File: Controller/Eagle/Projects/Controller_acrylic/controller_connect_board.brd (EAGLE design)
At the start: 185 x 33 mm, 13 parts, among them J1 GIMBAL_3PIN_MATCH_TDOCU, J2 GIMBAL_3PIN_MATCH_TDOCU, J3 GIMBAL_3PIN_MATCH_TDOCU, J4 GIMBAL_3PIN_MATCH_TDOCU, J5 GIMBAL_3PIN_MATCH_TDOCU

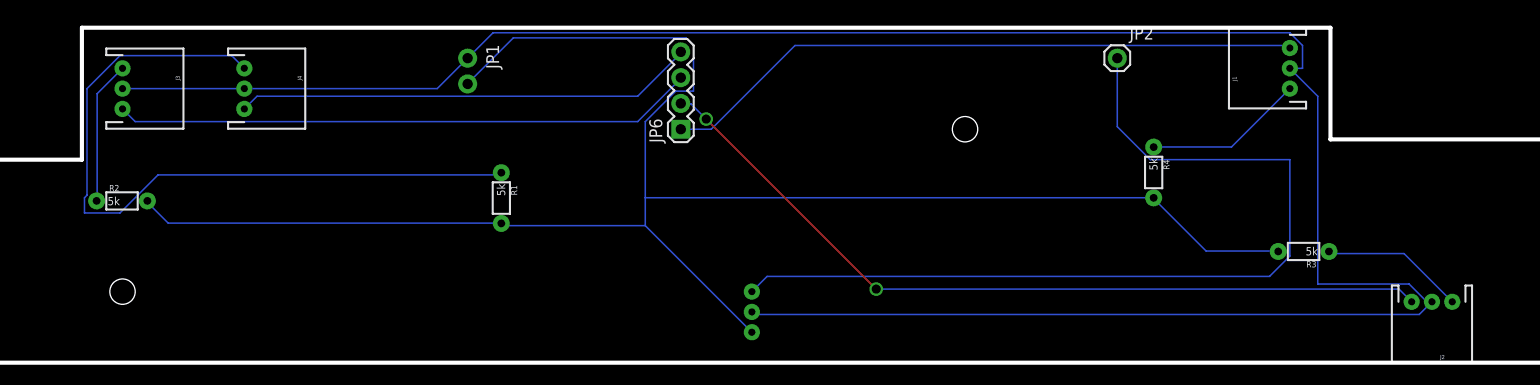
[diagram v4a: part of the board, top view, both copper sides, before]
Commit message: First test of connector board Ground and VDD were reversed on gimbal pins Made holes bigger
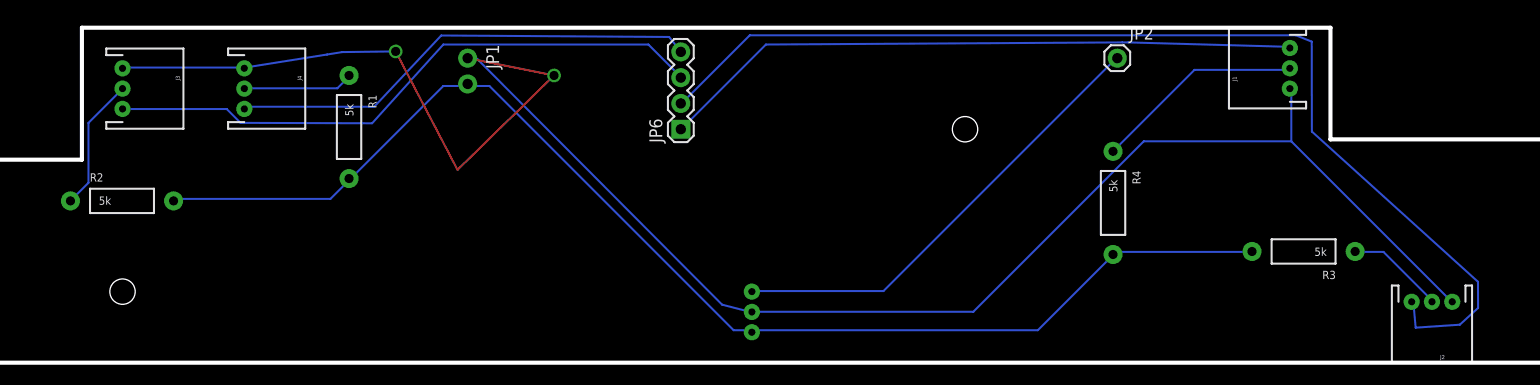
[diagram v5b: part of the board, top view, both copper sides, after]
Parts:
- J1, J2, J3, J4: value GIMBAL_3PIN_MATCH_TDOCU -> JST_3PIN_GND_VDD_SIG; device Controller:JST-3-PTH -> Controller:JST-3-PTH-REVERSE
- R1, R2, R3, R4: device SparkFun-Resistors:1/6W-RES -> SparkFun-Resistors:AXIAL-0.4
- moved R1 16.6 mm to (93.3, 45.2)
- moved R4 5.00 mm to (168.6, 37.7)
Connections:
- net N$5 renamed PITCH
- net N$6 renamed ROLL
- net N$7 renamed THROTTLE
- net N$8 renamed YAW
- net 3.3V: now also R1.P$2, R2.P$2, R3.P$2, R4.P$2; no longer R1.2, R2.2, R3.2, R4.2
- net GND: now also J1.1, J2.1, J3.1, J4.1; no longer J1.2, J2.2, J3.2, J4.2
- net N$1: now also J4.2, R1.P$1; no longer J4.1, R1.1
- net N$2: now also J3.2, R2.P$1; no longer J3.1, R2.1
- net N$3: now also J2.2, R3.P$1; no longer J2.1, R3.1
- net N$4: now also J1.2, R4.P$1; no longer J1.1, R4.1
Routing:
- net N$1: track 72.5 -> 10.9 mm
- net 3.3V: track 174.7 -> 124.8 mm
- net N$9: track 89.0 -> 45.5 mm
- net GND: track 224.4 -> 188.1 mm, vias 0 -> 2
- net ROLL: track 80.1 -> 108.0 mm, vias 2 -> 0
- net N$4: track 15.8 -> 20.8 mm
- net N$3: track 14.2 -> 9.69 mm
- net THROTTLE: track 57.4 -> 60.4 mm
- net YAW: track 45.4 -> 46.9 mm
- net N$2: track 14.1 -> 13.2 mm

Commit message: FORGOT THE BUTTON WOW WOW I...WOW
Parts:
- added BUTTON: (no value), SparkFun-Connectors:1X01
- added R5: ~10k, SparkFun-Resistors:AXIAL-0.4
- added U$2: BUTTON-TACTILE-SQUARE, Controller:BUTTON-TACTILE-SQUARE-ADAFRUIT1010
- R1, R2, R3, R4: value 5k -> 5k-8.2k
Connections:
- new net N$6: BUTTON.1, R5.P$2, U$2.S, U$2.S2
- net 3.3V: now also U$2.P, U$2.P2
- net GND: now also R5.P$1
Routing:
- net N$6: track 0.00 -> 36.9 mm
- net GND: track 188.1 -> 209.4 mm
- net N$9: track 45.5 -> 56.9 mm
- net 3.3V: track 124.8 -> 132.6 mm
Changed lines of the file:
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@@
 <element name="J3" library="Controller" package="JST-3-PTH-REVERSE" value="JST_3PIN_GND_VDD_SIG" x="71" y="49" rot="R270"/>
 <element name="J4" library="Controller" package="JST-3-PTH-REVERSE" value="JST_3PIN_GND_VDD_SIG" x="83" y="49" rot="R270"/>
-<element name="R1" library="SparkFun-Resistors" package="AXIAL-0.4" value="5k" x="93.318003125" y="45.219046875" rot="R270"/>
-<element name="R2" library="SparkFun-Resistors" package="AXIAL-0.4" value="5k" x="70.949403125" y="37.939940625"/>
-<element name="R3" library="SparkFun-Resistors" package="AXIAL-0.4" value="5k" x="187.352325" y="32.957490625" rot="R180"/>
-<element name="R4" library="SparkFun-Resistors" package="AXIAL-0.4" value="5k" x="168.58266875" y="37.739028125" rot="R270"/>
+<element name="R1" library="SparkFun-Resistors" package="AXIAL-0.4" value="5k-8.2k" x="93.318003125" y="45.219046875" rot="R270"/>
+<element name="R2" library="SparkFun-Resistors" package="AXIAL-0.4" value="5k-8.2k" x="70.949403125" y="37.939940625"/>
+<element name="R3" library="SparkFun-Resistors" package="AXIAL-0.4" value="5k-8.2k" x="187.352325" y="32.957490625" rot="R180"/>
+<element name="R4" library="SparkFun-Resistors" package="AXIAL-0.4" value="5k-8.2k" x="168.58266875" y="37.739028125" rot="R270"/>
 <element name="JP6" library="SparkFun-Connectors" package="1X04" value="" x="126" y="45" rot="R90"/>
 <element name="JP1" library="SparkFun-Connectors" package="1X02_NO_SILK" value="" x="105" y="52" rot="R270"/>
@@
 <element name="JP2" library="SparkFun-Connectors" package="1X01" value="" x="169" y="52"/>
 <element name="U$1" library="Controller" package="CONNECTOR_BOARD_OUTLINE" value="" x="0" y="0"/>
+<element name="U$2" library="Controller" package="BUTTON-TACTILE-SQUARE-ADAFRUIT1010" value="BUTTON-TACTILE-SQUARE" x="152.719" y="31.166" rot="R180"/>
+<element name="BUTTON" library="SparkFun-Connectors" package="1X01" value="" x="156.66" y="49.897"/>
+<element name="R5" library="SparkFun-Resistors" package="AXIAL-0.4" value="~10k" x="143.013" y="49.942"/>
 </elements>
 <signals>
@@
 <wire x1="82.855" y1="51.075" x2="83" y2="51" width="0.2" layer="16"/>
 <wire x1="130.071" y1="27.715" x2="132.795" y2="27.013" width="0.2" layer="16"/>
-<wire x1="105.968" y1="51.9" x2="130.071" y2="27.715" width="0.2" layer="16"/>
+<wire x1="105.968" y1="51.9" x2="122.40503125" y2="35.40705" width="0.2" layer="16"/>
+<wire x1="122.40503125" y1="35.40705" x2="130.071" y2="27.715" width="0.2" layer="16"/>
 <wire x1="132.795" y1="27.013" x2="133" y2="27" width="0.2" layer="16"/>
 <wire x1="105.968" y1="51.9" x2="105" y2="52" width="0.2" layer="16"/>
@@
 <wire x1="83.082" y1="51.075" x2="83" y2="51" width="0.2" layer="16"/>
 <wire x1="171.612" y1="43.811" x2="186.14" y2="43.811" width="0.2" layer="16"/>
-<wire x1="154.814" y1="27.013" x2="171.612" y2="43.811" width="0.2" layer="16"/>
-<wire x1="133.022" y1="27.013" x2="154.814" y2="27.013" width="0.2" layer="16"/>
 <wire x1="133.022" y1="27.013" x2="133" y2="27" width="0.2" layer="16"/>
 <via x="97.909" y="52.665" extent="1-16" drill="0.9"/>
@@
 <wire x1="97.909" y1="52.665" x2="104" y2="41" width="0.2" layer="1"/>
 <wire x1="104" y1="41" x2="113.515" y2="50.296" width="0.2" layer="1"/>
+<contactref element="R5" pad="P$1"/>
+<wire x1="171.612" y1="43.811" x2="164" y2="33" width="0.2" layer="16"/>
+<wire x1="164" y1="33" x2="159.184" y2="31.052" width="0.2" layer="16"/>
+<wire x1="159.184" y1="31.052" x2="144.977" y2="30.956" width="0.2" layer="16"/>
+<wire x1="144.977" y1="30.956" x2="141.977" y2="26.96" width="0.2" layer="16"/>
+<wire x1="141.977" y1="26.96" x2="133" y2="27" width="0.2" layer="16"/>
+<wire x1="144.977" y1="30.956" x2="137.933" y2="49.942" width="0.2" layer="16"/>
 </signal>
 <signal name="N$1">
@@
 <wire x1="104.874" y1="49.259" x2="105" y2="49.46" width="0.2" layer="16"/>
 <wire x1="93.524" y1="40.179" x2="93.318003125" y2="40.139046875" width="0.2" layer="16"/>
-<wire x1="161.17" y1="25.197" x2="133.022" y2="25.197" width="0.2" layer="16"/>
+<wire x1="161.17" y1="25.197" x2="146" y2="25.197" width="0.2" layer="16"/>
+<wire x1="146" y1="25.197" x2="133.022" y2="25.197" width="0.2" layer="16"/>
 <wire x1="168.434" y1="32.461" x2="161.17" y2="25.197" width="0.2" layer="16"/>
 <wire x1="133.022" y1="25.197" x2="133" y2="25" width="0.2" layer="16"/>
@@
 <wire x1="105.101" y1="49.259" x2="105" y2="49.46" width="0.2" layer="16"/>
 <wire x1="132.795" y1="25.197" x2="133" y2="25" width="0.2" layer="16"/>
+<contactref element="U$2" pad="P2"/>
+<wire x1="146.719" y1="28.666" x2="146" y2="25.197" width="0.2" layer="16"/>
+<contactref element="U$2" pad="P"/>
+<wire x1="161.17" y1="25.197" x2="158.719" y2="28.666" width="0.2" layer="16"/>
 </signal>
 <signal name="PITCH">
@@
 <contactref element="J5" pad="3"/>
 <contactref element="JP2" pad="1"/>
-<wire x1="145.961" y1="29.056" x2="133.022" y2="29.056" width="0.2" layer="16"/>
-<wire x1="168.888" y1="51.983" x2="145.961" y2="29.056" width="0.2" layer="16"/>
 <wire x1="133.022" y1="29.056" x2="133" y2="29" width="0.2" layer="16"/>
 <wire x1="168.888" y1="51.983" x2="169" y2="52" width="0.2" layer="16"/>
+<wire x1="133.022" y1="29.056" x2="135.253" y2="51.966" width="0.2" layer="16"/>
+<wire x1="135.253" y1="51.966" x2="169" y2="52" width="0.2" layer="16"/>
+</signal>
+<signal name="N$6">
+<contactref element="U$2" pad="S2"/>
+<contactref element="BUTTON" pad="1"/>
+<contactref element="R5" pad="P$2"/>
+<wire x1="156.66" y1="49.897" x2="148.093" y2="49.942" width="0.2" layer="16"/>
+<wire x1="148.093" y1="49.942" x2="146.719" y2="33.666" width="0.2" layer="16"/>
+<contactref element="U$2" pad="S"/>
+<wire x1="146.719" y1="33.666" x2="158.719" y2="33.666" width="0.2" layer="16"/>
 </signal>
 </signals>
